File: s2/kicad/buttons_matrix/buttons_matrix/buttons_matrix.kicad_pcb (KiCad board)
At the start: 2 copper layers, 94 parts, among them J1 to_rpi, J10 B_Col_4_A, J11 B_Col_4_B, J12 B_Col_5_A, J13 B_Col_5_B, J14 B_Col_6_A, J15 B_Col_6_B, J16 B_Col_7_A, J17 B_Col_7_B, J18 to_button_matrix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

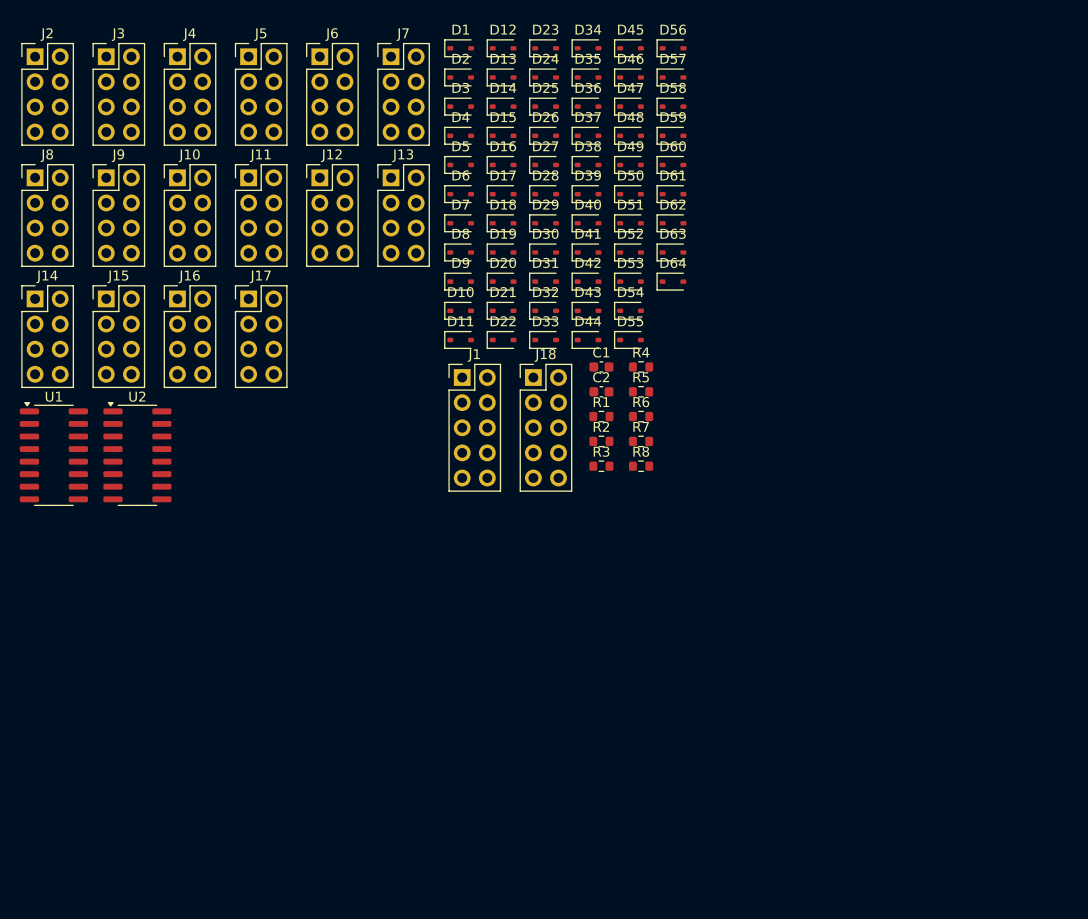
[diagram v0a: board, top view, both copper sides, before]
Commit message: added s2-osc front eurorack
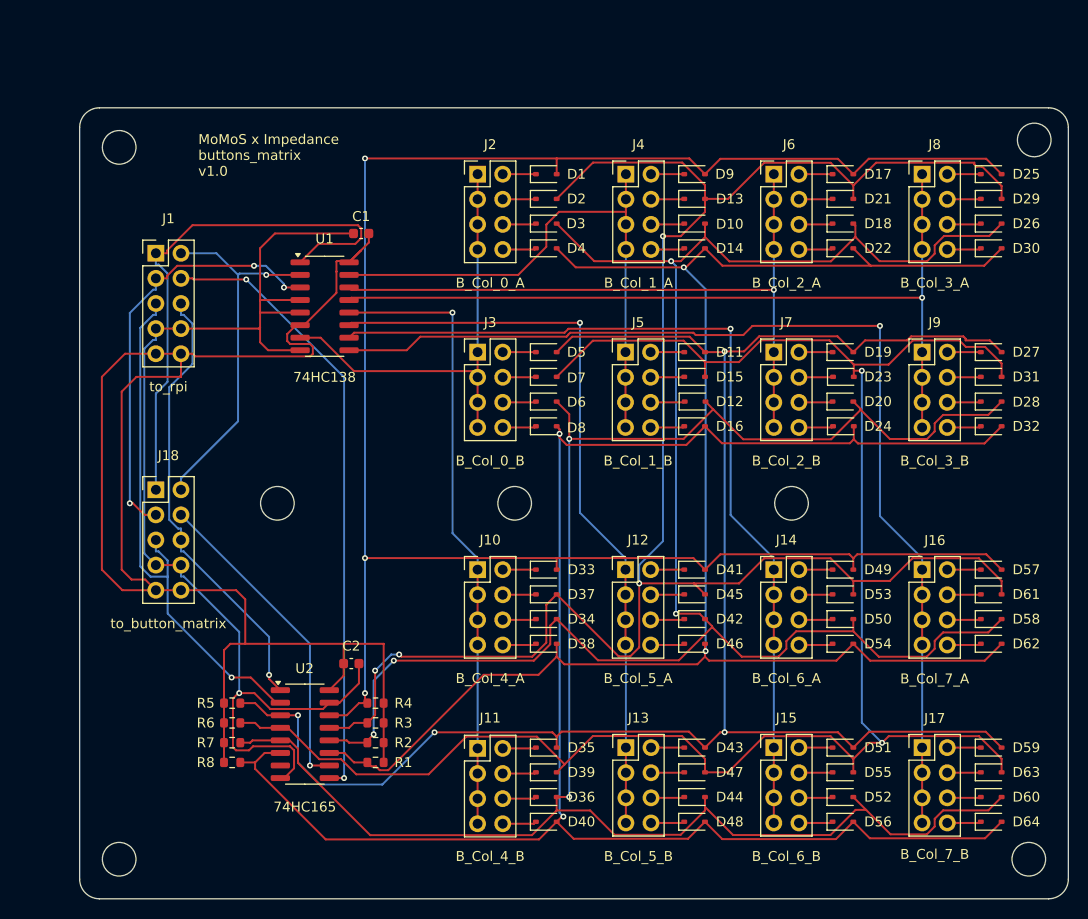
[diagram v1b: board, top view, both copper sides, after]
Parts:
- moved J8 89.7 mm to (110.2, 31.7)
- moved J9 84.4 mm to (110.2, 49.7)
- moved J17 81.8 mm to (110.2, 89.7)
- moved J15 81.3 mm to (95.2, 89.7)
- moved J16 80.1 mm to (110.2, 71.7)
- moved D56 80.1 mm to (102.2, 97.2)
- moved J14 79.6 mm to (95.2, 71.7)
- moved D60 71.6 mm to (117.2, 94.7)
- moved D36 70.0 mm to (72.2, 94.7)
- moved D59 69.7 mm to (117.2, 89.7)
- moved D48 69.7 mm to (87.2, 97.2)
- moved D35 67.9 mm to (72.2, 89.7)
- moved D47 67.6 mm to (87.2, 92.2)
- moved D64 63.4 mm to (117.2, 97.2)
- moved J13 62.3 mm to (80.2, 89.7)
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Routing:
- net /B_Row_0: track 0.00 -> 197.6 mm, vias 0 -> 3
- net /B_Row_1: track 0.00 -> 195.0 mm, vias 0 -> 4
- net /B_Row_6: track 0.00 -> 189.6 mm, vias 0 -> 2
- net /B_Row_5: track 0.00 -> 188.3 mm, vias 0 -> 2
- net /B_Row_2: track 0.00 -> 183.6 mm, vias 0 -> 4
- net /B_Row_7: track 0.00 -> 178.5 mm, vias 0 -> 2
- net /B_Row_4: track 0.00 -> 177.7 mm, vias 0 -> 4
- net /B_Row_3: track 0.00 -> 169.3 mm, vias 0 -> 2
- net +3.3V: track 0.00 -> 159.4 mm
- net GND: track 0.00 -> 117.7 mm, vias 0 -> 1
- net /B_Col_7: track 0.00 -> 107.0 mm, vias 0 -> 1
- net /B_Col_6: track 0.00 -> 90.8 mm, vias 0 -> 1
- net /B_Col_3: track 0.00 -> 83.7 mm, vias 0 -> 1
- net /B_Col_5: track 0.00 -> 76.0 mm, vias 0 -> 1
- net /B_Col_2: track 0.00 -> 68.7 mm, vias 0 -> 1
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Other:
- board outline added: 100 x 80 mm
- board text added: "MoMoS x Impedance buttons_matrix v1.0"
